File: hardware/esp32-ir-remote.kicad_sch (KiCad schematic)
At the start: 65 parts, among them J1 ESP32-WROOM-32E-Breakout, J2 USB_C_Receptacle_USB2.0_14P, Q1 Q_NPN_BCE, Q2 Q_NPN_BCE, Q3 IRLML6344, Q4 2N7002, Q5 2N7002, SW1 RESET, SW2 BOOT, U1 AP63203WU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

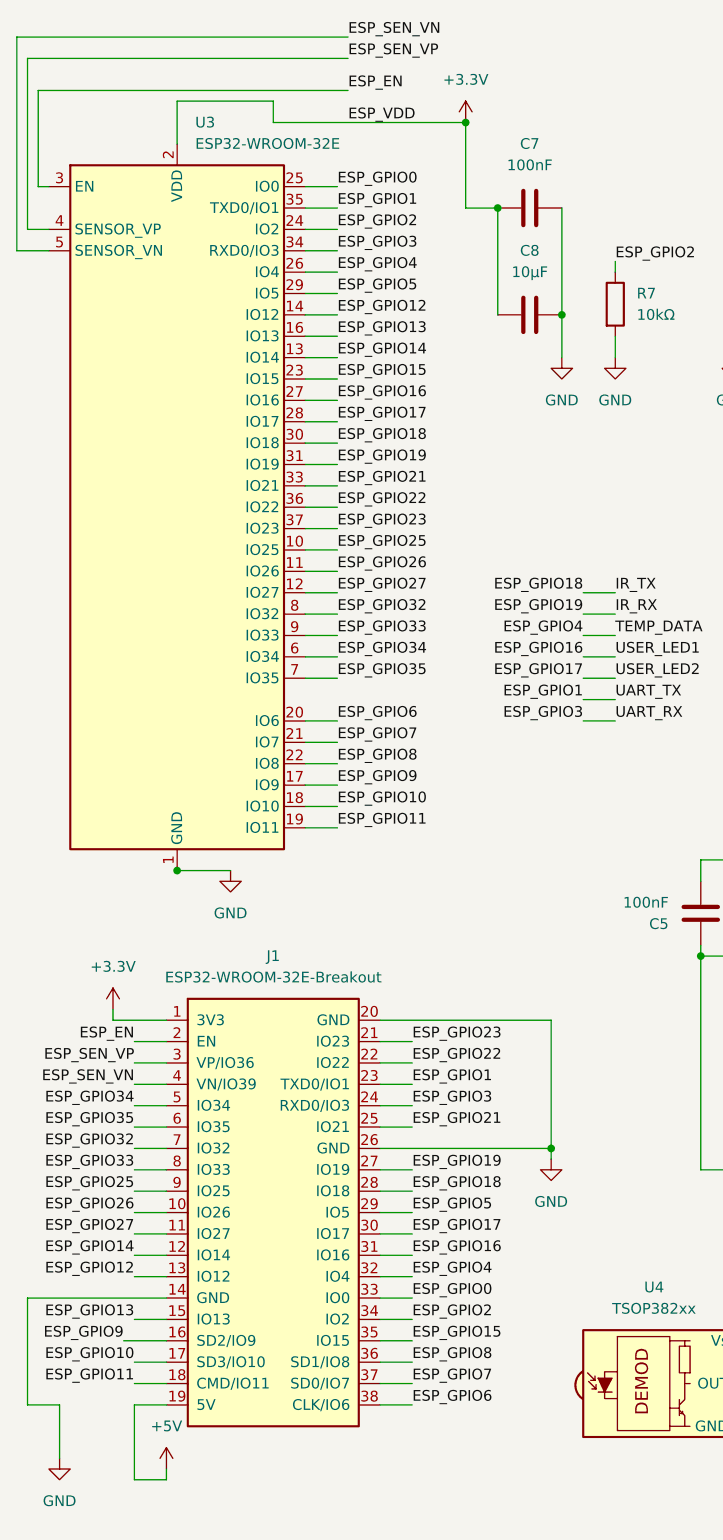
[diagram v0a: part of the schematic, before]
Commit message: v1.2: remove J1 DevKitC debug breakout header (38 pins)
Removed J1, its 4 power symbols, 47 harness wires, 33 net labels and a
junction (scripted s-expr surgery; the J1 harness was verified fully
self-contained first - no boundary-crossing wires). The 22 GPIO nets that
existed only for the breakout (5, 6-11 flash, 12-14, 21-23, 25-27, 32-35,
SENSOR_VP/VN) had their U3-side stubs+labels removed and explicit
no_connect flags placed; 12 of them come back in the v1.2 connection
points (Qwiic 21/22, spare header 23/25/26/32/33/34, JTAG 12/13/14/15).
GPIO2/15 keep their strapping pulldowns (R7/R8); GPIO6-11 flash pins are
now not broken out anywhere, resolving the H1.4 'confirm J1 GPIO6-11
intent' item.

Verified: net partition identical to HEAD minus exactly J1's 38 pins and
the 22 single-pin label nets; ERC 0 errors, 7 warnings (all the documented
deliberate dual-label pattern).
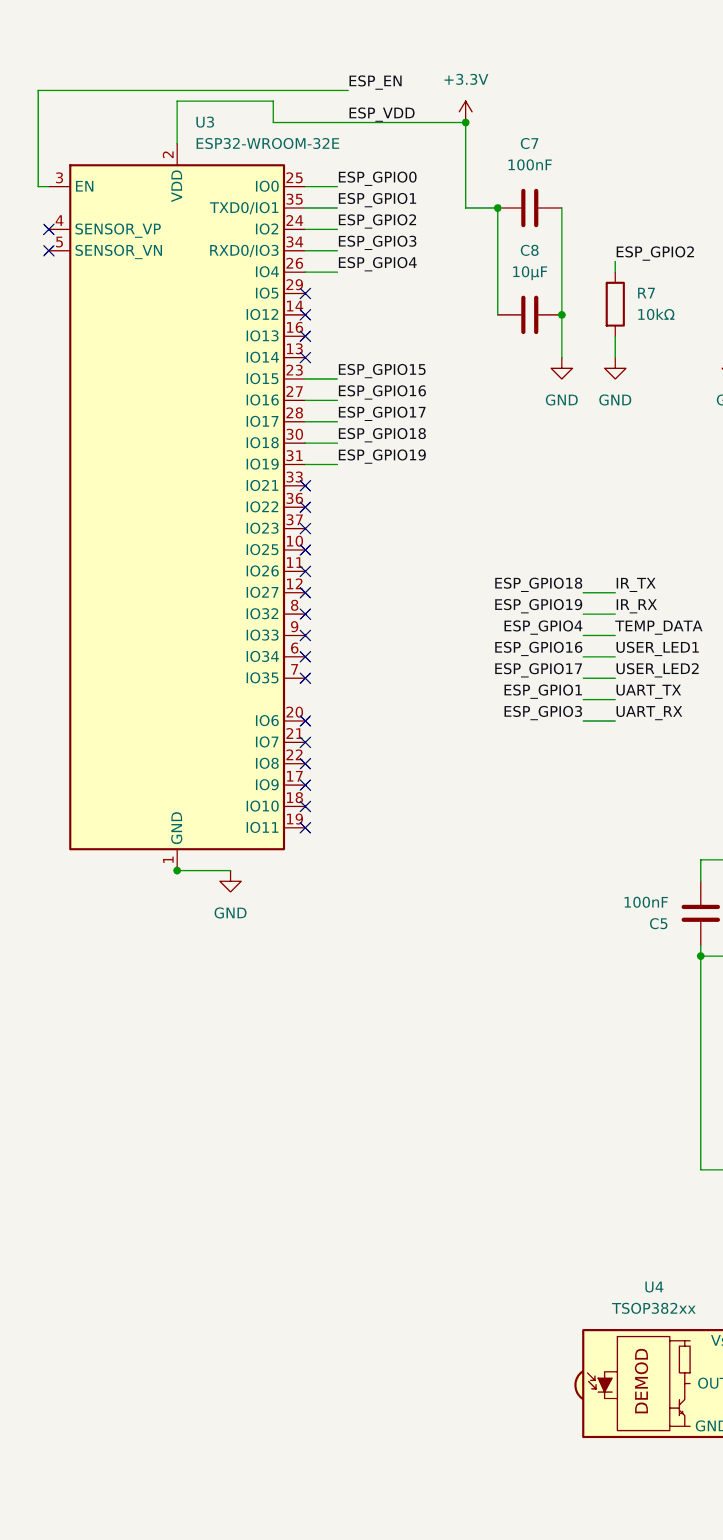
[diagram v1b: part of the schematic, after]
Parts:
- removed J1: ESP32-WROOM-32E-Breakout, lib:PinHeader_2x19_P2.54mm_DevKitC, symbol ESP32-WROOM-32E-Breakout:ESP32-WROOM-32E-Breakout
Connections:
- net ESP_GPIO10: no longer names the net of U3.18 (IO10)
- net ESP_GPIO11: no longer names the net of U3.19 (IO11)
- net ESP_GPIO12: no longer names the net of U3.14 (IO12)
- net ESP_GPIO13: no longer names the net of U3.16 (IO13)
- net ESP_GPIO14: no longer names the net of U3.13 (IO14)
- net ESP_GPIO21: no longer names the net of U3.33 (IO21)
- net ESP_GPIO22: no longer names the net of U3.36 (IO22)
- net ESP_GPIO23: no longer names the net of U3.37 (IO23)
- net ESP_GPIO25: no longer names the net of U3.10 (IO25)
- net ESP_GPIO26: no longer names the net of U3.11 (IO26)
- net ESP_GPIO27: no longer names the net of U3.12 (IO27)
- net ESP_GPIO32: no longer names the net of U3.8 (IO32)
- net ESP_GPIO33: no longer names the net of U3.9 (IO33)
- net ESP_GPIO34: no longer names the net of U3.6 (IO34)
- net ESP_GPIO35: no longer names the net of U3.7 (IO35)
- net ESP_GPIO5: no longer names the net of U3.29 (IO5)
- net ESP_GPIO6: no longer names the net of U3.20 (IO6)
- net ESP_GPIO7: no longer names the net of U3.21 (IO7)
- net ESP_GPIO8: no longer names the net of U3.22 (IO8)
- net ESP_GPIO9: no longer names the net of U3.17 (IO9)
- net ESP_SEN_VN: no longer names the net of U3.5 (SENSOR_VN)
- net ESP_SEN_VP: no longer names the net of U3.4 (SENSOR_VP)
- no-connect marks 4 -> 26

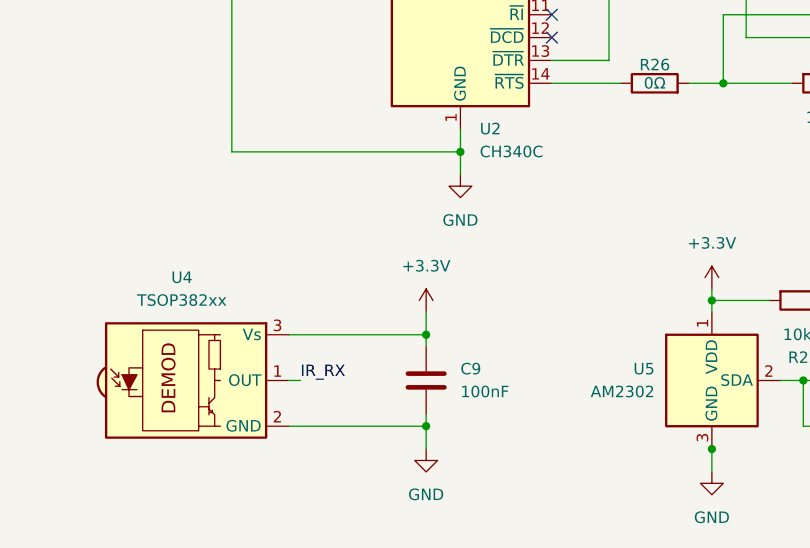
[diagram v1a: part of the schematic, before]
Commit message: v1.2: add TSOP Vs RC filter (H1.4 MED fix)
+3.3V -> R27 100R (1206, C17901 Basic) -> new IR_RX_VS net -> U4 Vs, with
the existing C9 100nF now decoupling the filtered node (datasheet's
recommended supply ripple filter for the TSOP receiver). PWR_FLAG #FLG04
marks the node as intentionally resistor-fed (KiCad power_pin_not_driven).

Netlist: /IR_RX_VS = {R27.2, U4.3, C9.1}; C9.2 stays on GND; no other nets
touched. ERC 0 errors.
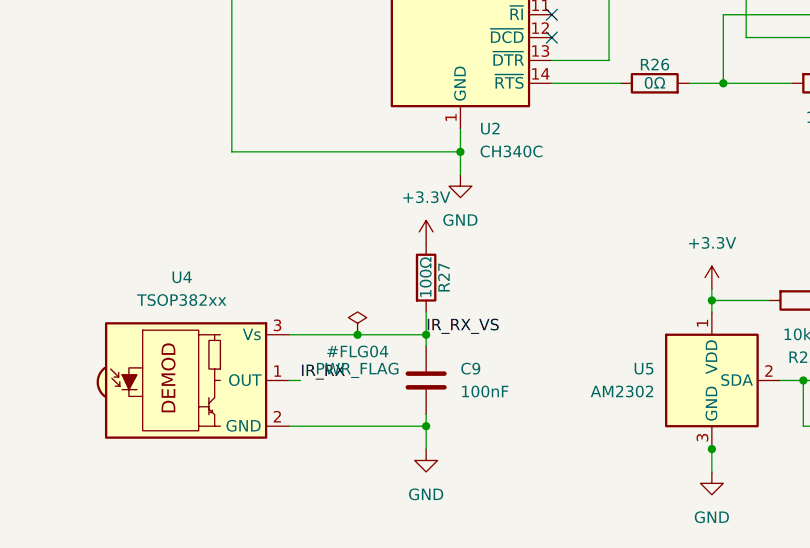
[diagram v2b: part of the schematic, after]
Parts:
- added R27: 100Ω, Resistor_SMD:R_1206_3216Metric, symbol Device:R
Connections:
- net +3.3V: now also R27.1; no longer C9.1, U4.3 (Vs)
- new net IR_RX_VS: C9.1, R27.2, U4.3 (Vs)

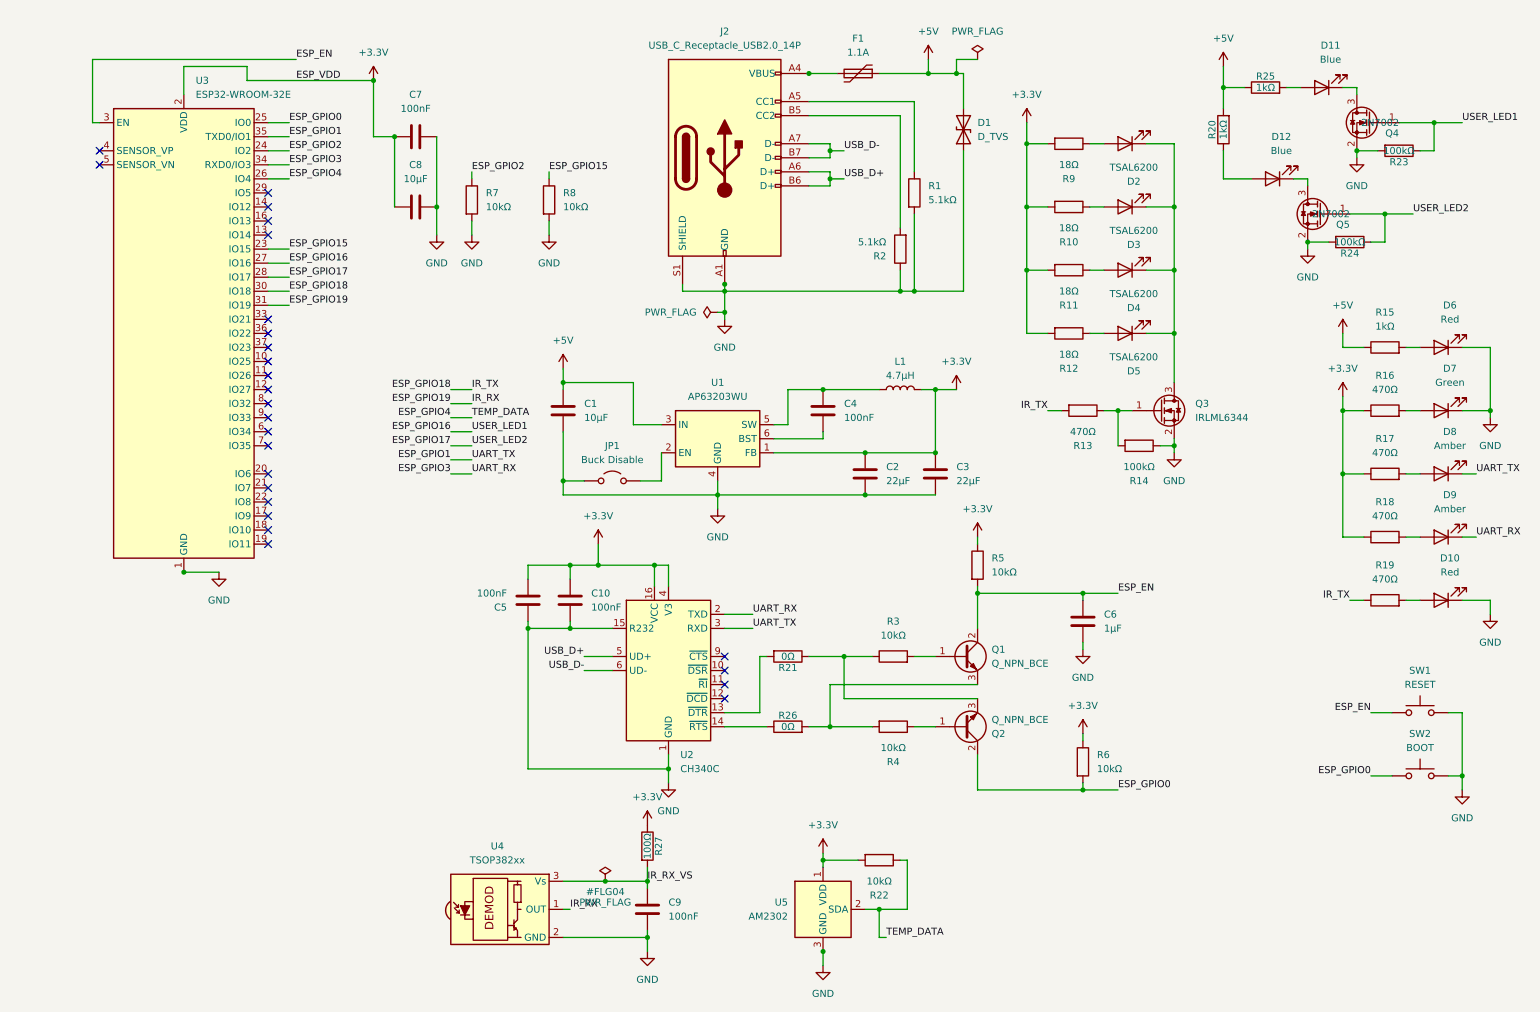
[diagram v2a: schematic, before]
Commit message: v1.2: add connection points - Qwiic, spare-GPIO header, ext-IR header, JTAG
J3 Qwiic (JST-SH SM04B-SRSS-TB, C160404): GND/3V3/SDA=GPIO21/SCL=GPIO22,
with R28/R29 4.7k pull-up footprints (1206, C17936, DNP - most Qwiic
modules carry their own).
J4 spare 2x5 2.54mm: 3V3, 5V, GPIO23/25/26/32/33/34, 2x GND.
J5 ext-IR 2-pin: pin1 -> R30 18R series footprint (C17955, DNP) -> +3.3V
(net EXT_IR_A); pin2 -> Q3 drain (the LED-cathode net, now labelled
IR_DRAIN). External emitter switches with the onboard array per spec.
J6 JTAG 2x5 (DNP), ARM 10-pin layout: 3V3/TMS=GPIO14/TCK=GPIO13/
TDO=GPIO15/TDI=GPIO12/EN=nRESET + 3x GND, key pin NC.
The 11 reused GPIOs got their no_connects removed and U3-side labels
restored; netlist confirms each: e.g. ESP_GPIO21={U3.33,J3.3,R28.2}.

kicad-edit MCP bugs worked around: add_schematic_component ignores its
angle param (R30 placed vertical+rewired); KiCad 9 netlister drops/
misnames label-less 2-pin nets (ERC false 'wire_dangling', net absent) -
fixed by naming the net (EXT_IR_A). ERC 0 errors / 7 deliberate dual-label
warnings; partition vs HEAD verified (additions only). File re-formatted
after MCP flattening.
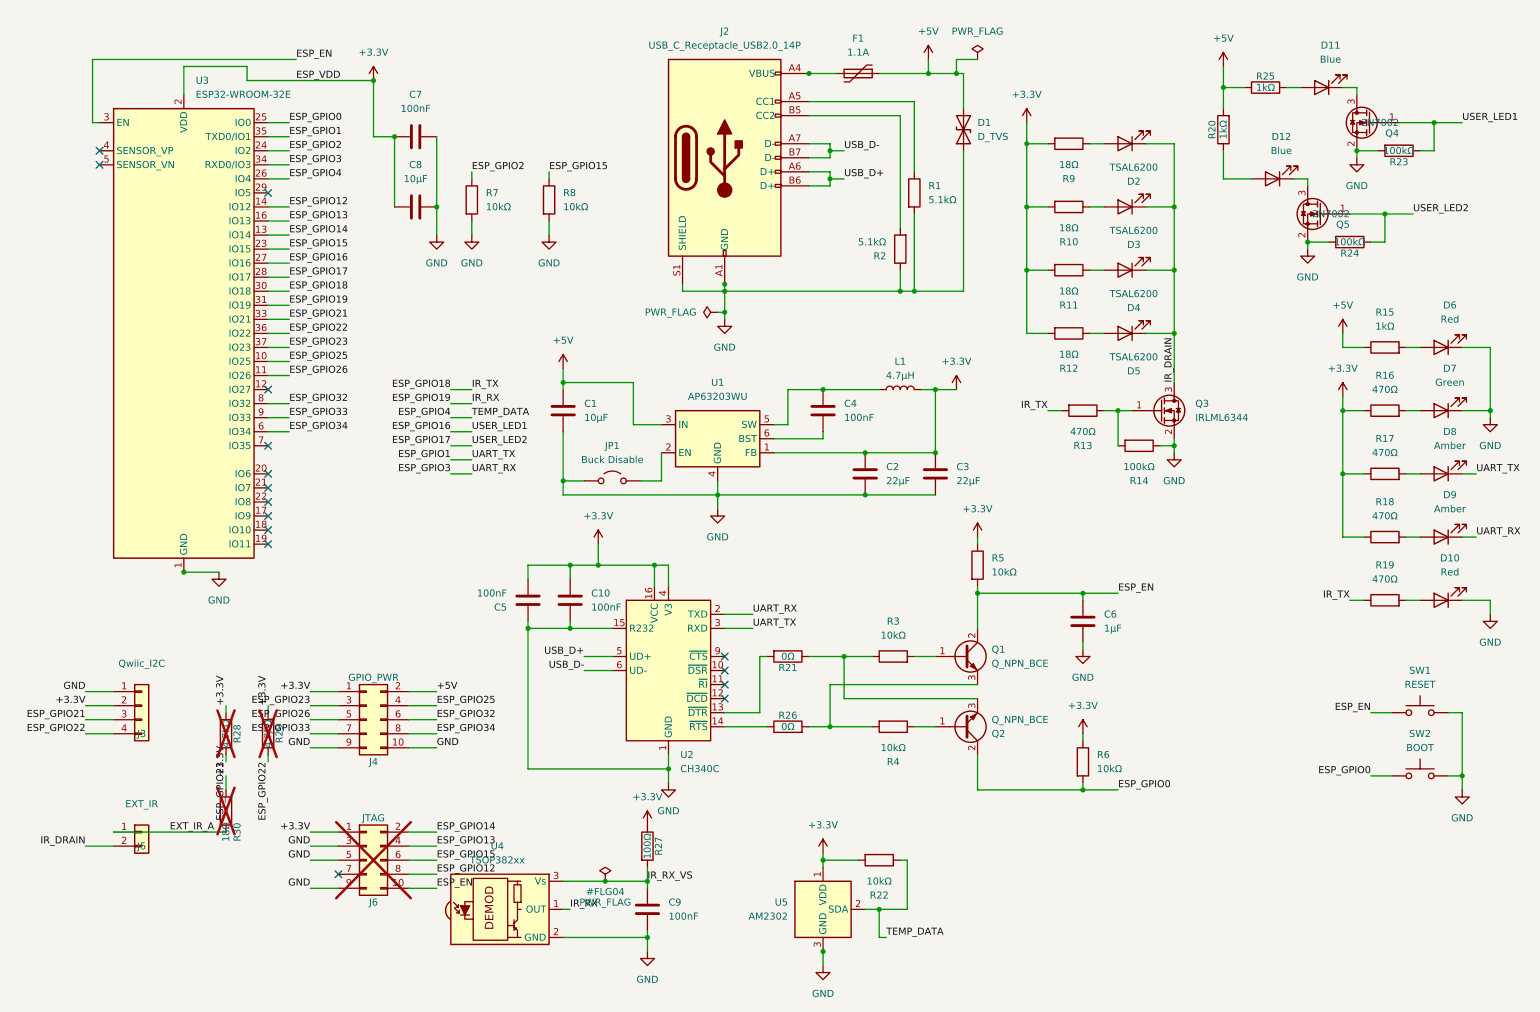
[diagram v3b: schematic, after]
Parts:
- added J3: Qwiic_I2C, Connector_JST:JST_SH_SM04B-SRSS-TB_1x04-1MP_P1.00mm_Horizontal, symbol Connector_Generic:Conn_01x04
- added J4: GPIO_PWR, Connector_PinHeader_2.54mm:PinHeader_2x05_P2.54mm_Vertical, symbol Connector_Generic:Conn_02x05_Odd_Even
- added J5: EXT_IR, Connector_PinHeader_2.54mm:PinHeader_1x02_P2.54mm_Vertical, symbol Connector_Generic:Conn_01x02
- added J6: JTAG, Connector_PinHeader_2.54mm:PinHeader_2x05_P2.54mm_Vertical, symbol Connector_Generic:Conn_02x05_Odd_Even
- added R28, R29: 4.7kΩ, Resistor_SMD:R_1206_3216Metric, symbol Device:R
- added R30: 18Ω, Resistor_SMD:R_1206_3216Metric, symbol Device:R
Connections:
- net +3.3V: now also J3.2 (Pin_2), J4.1 (Pin_1), J6.1 (Pin_1), R28.1, R29.1, R30.1
- net +5V: now also J4.2 (Pin_2)
- net ESP_EN: now also J6.10 (Pin_10)
- net ESP_GPIO15: now also J6.6 (Pin_6)
- net GND: now also J3.1 (Pin_1), J4.10 (Pin_10), J4.9 (Pin_9), J6.3 (Pin_3), J6.5 (Pin_5), J6.9 (Pin_9)
- net IR_DRAIN: now reaches D2.1 (K), D3.1 (K), D4.1 (K), D5.1 (K), Q3.3 (D)
- net IR_DRAIN: now also J5.2 (Pin_2)
- net ESP_GPIO25: now reaches U3.10 (IO25)
- net ESP_GPIO25: now also J4.4 (Pin_4)
- net ESP_GPIO26: now reaches U3.11 (IO26)
- net ESP_GPIO26: now also J4.5 (Pin_5)
- net ESP_GPIO14: now reaches U3.13 (IO14)
- net ESP_GPIO14: now also J6.2 (Pin_2)
- net ESP_GPIO12: now reaches U3.14 (IO12)
- net ESP_GPIO12: now also J6.8 (Pin_8)
- net ESP_GPIO13: now reaches U3.16 (IO13)
- net ESP_GPIO13: now also J6.4 (Pin_4)
- net ESP_GPIO21: now reaches U3.33 (IO21)
- net ESP_GPIO21: now also J3.3 (Pin_3), R28.2
- net ESP_GPIO22: now reaches U3.36 (IO22)
- net ESP_GPIO22: now also J3.4 (Pin_4), R29.2
- net ESP_GPIO23: now reaches U3.37 (IO23)
- net ESP_GPIO23: now also J4.3 (Pin_3)
- net ESP_GPIO34: now reaches U3.6 (IO34)
- net ESP_GPIO34: now also J4.8 (Pin_8)
- net ESP_GPIO32: now reaches U3.8 (IO32)
- net ESP_GPIO32: now also J4.6 (Pin_6)
- net ESP_GPIO33: now reaches U3.9 (IO33)
- net ESP_GPIO33: now also J4.7 (Pin_7)
- new net EXT_IR_A: J5.1 (Pin_1), R30.2
- no-connect marks 26 -> 16

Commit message: v1.2 wrap-up: regenerate BOM from schematic, demote BOM.md, roadmap
BOM CSV regenerated with DNP column; only the 3 hand-solder pin headers
lack LCSC (deliberate). Restored LCSC on the 8 symbol-swapped parts (the
replace tool drops custom fields) and fixed two more latent code bugs
found while re-verifying every code on LCSC/JLCPCB: Q3 IRLML6344 carried
C8545 (the 2N7002 code) -> C53550; R14 100k and R15 1k carried 0805 codes
on 1206 footprints -> C17900 / C4410 (both Basic, >900k stock).

BOM.md demoted to rationale-only with a stale-data warning banner.
ROADMAP: v1.2 change set marked done; kicad-edit MCP bug list documented
(angle param ignored, field-dropping replace, file flattening, KiCad 9
label-less-net netlister quirk, label justification offsets upstream #234,
get_board_2d_view layers #235).
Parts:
- Q3: LCSC C8545 -> C53550
- Q4, Q5: LCSC (none) -> C8545
- R14: LCSC C149504 -> C17900
- R15: LCSC C17513 -> C4410
- R20, R25: LCSC (none) -> C17513
- R21, R26: LCSC (none) -> C21189
- R23, R24: LCSC (none) -> C25803
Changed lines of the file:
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@@
 			(effects (font (size 1.27 1.27)) (hide yes))
 		)
-		(property "LCSC" "C8545"
+		(property "LCSC" "C53550"
 			(at 212.09 87.63 0)
 			(effects (font (size 1.27 1.27)) (hide yes))
@@
 			(effects (font (size 1.27 1.27)) (hide yes))
 		)
-		(property "LCSC" "C149504"
+		(property "LCSC" "C17900"
 			(at 208.28 93.98 0)
 			(effects (font (size 1.27 1.27)) (hide yes))
@@
 			(effects (font (size 1.27 1.27)) (hide yes))
 		)
-		(property "LCSC" "C17513"
+		(property "LCSC" "C4410"
 			(at 252.73 76.2 0)
 			(effects (font (size 1.27 1.27)) (hide yes))
@@
 			(effects (font (size 1.27 1.27)) (hide yes))
 		)
+    (property "LCSC" "C25803" (at 255.27 40.64 0)
+      (effects (font (size 1.27 1.27)) (hide yes))
+    )
 		(instances
 			(project "project" (path "/" (reference "R23") (unit 1)))
@@
 			(effects (font (size 1.27 1.27)) (hide yes))
 		)
+    (property "LCSC" "C17513" (at 223.52 36.83 0)
+      (effects (font (size 1.27 1.27)) (hide yes))
+    )
 		(instances
 			(project "project" (path "/" (reference "R20") (unit 1)))
@@
 			(effects (font (size 1.27 1.27)) (hide yes))
 		)
+    (property "LCSC" "C21189" (at 144.78 132.08 0)
+      (effects (font (size 1.27 1.27)) (hide yes))
+    )
 		(instances
 			(project "project" (path "/" (reference "R21") (unit 1)))
@@
 			(effects (font (size 1.27 1.27)) (hide yes))
 		)
+    (property "LCSC" "C25803" (at 246.38 57.15 0)
+      (effects (font (size 1.27 1.27)) (hide yes))
+    )
 		(instances
 			(project "project" (path "/" (reference "R24") (unit 1)))
@@
 			(effects (font (size 1.27 1.27)) (hide yes))
 		)
+    (property "LCSC" "C17513" (at 231.14 29.21 0)
+      (effects (font (size 1.27 1.27)) (hide yes))
+    )
 		(instances
 			(project "project" (path "/" (reference "R25") (unit 1)))
@@
 			(effects (font (size 1.27 1.27)) (hide yes))
 		)
+    (property "LCSC" "C21189" (at 144.78 144.78 0)
+      (effects (font (size 1.27 1.27)) (hide yes))
+    )
 		(instances
 			(project "project" (path "/" (reference "R26") (unit 1)))
@@
 			(effects (font (size 1.27 1.27)) (hide yes))
 		)
+    (property "LCSC" "C8545" (at 250.19 35.56 0)
+      (effects (font (size 1.27 1.27)) (hide yes))
+    )
 		(instances
 			(project "project" (path "/" (reference "Q4") (unit 1)))
@@
 			(effects (font (size 1.27 1.27)) (hide yes))
 		)
+    (property "LCSC" "C8545" (at 241.3 52.07 0)
+      (effects (font (size 1.27 1.27)) (hide yes))
+    )
 		(instances
 			(project "project" (path "/" (reference "Q5") (unit 1)))
